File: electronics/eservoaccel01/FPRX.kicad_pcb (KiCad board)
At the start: 2 copper layers, 25 x 37 mm, 83 parts, among them IC1 ST490, IC3 ATMEGA328P-M, K1 CONN_3, K2 CONN_3, K3 CONN_3, K4 CONN_3, P1 CONN_6, P2 CONN_1, X1 RESONATOR_16MHz

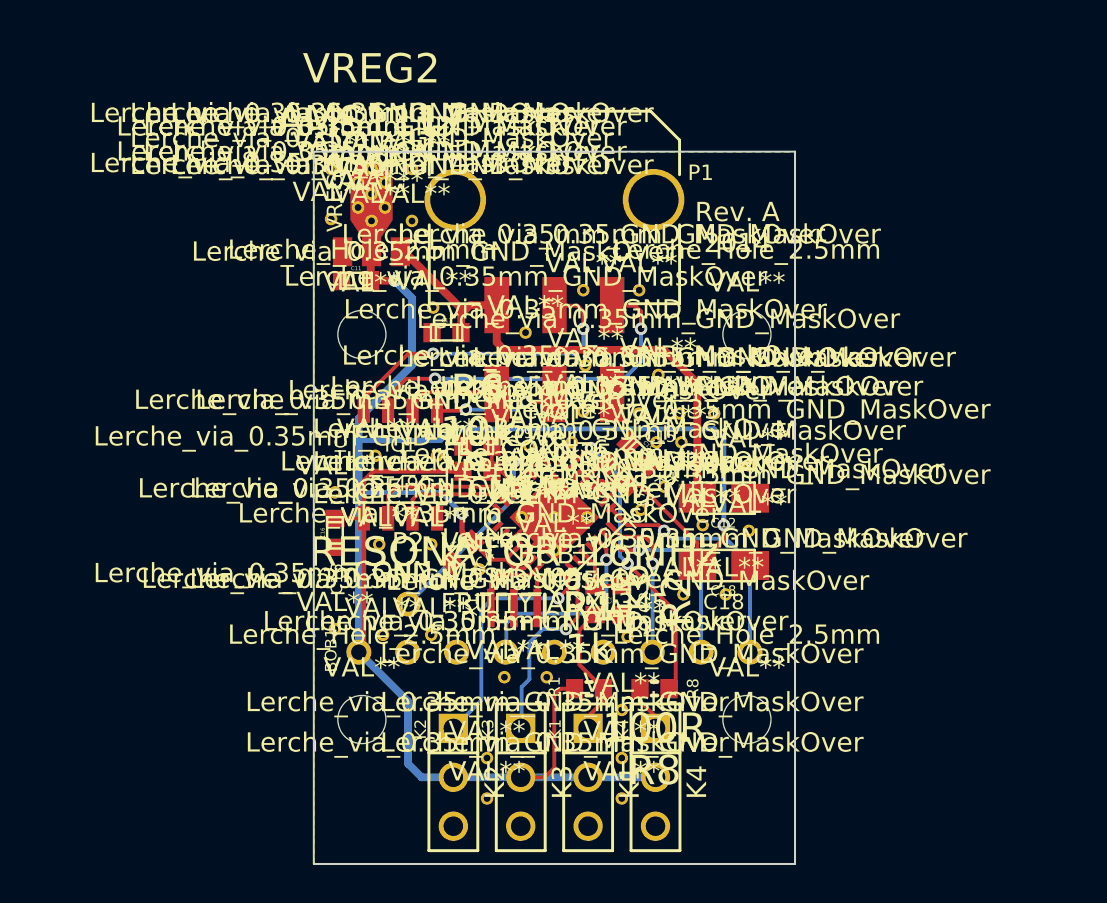
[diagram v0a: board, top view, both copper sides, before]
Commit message: Removed unused components from schematic, added WS2812 LED, changed C18 to C17
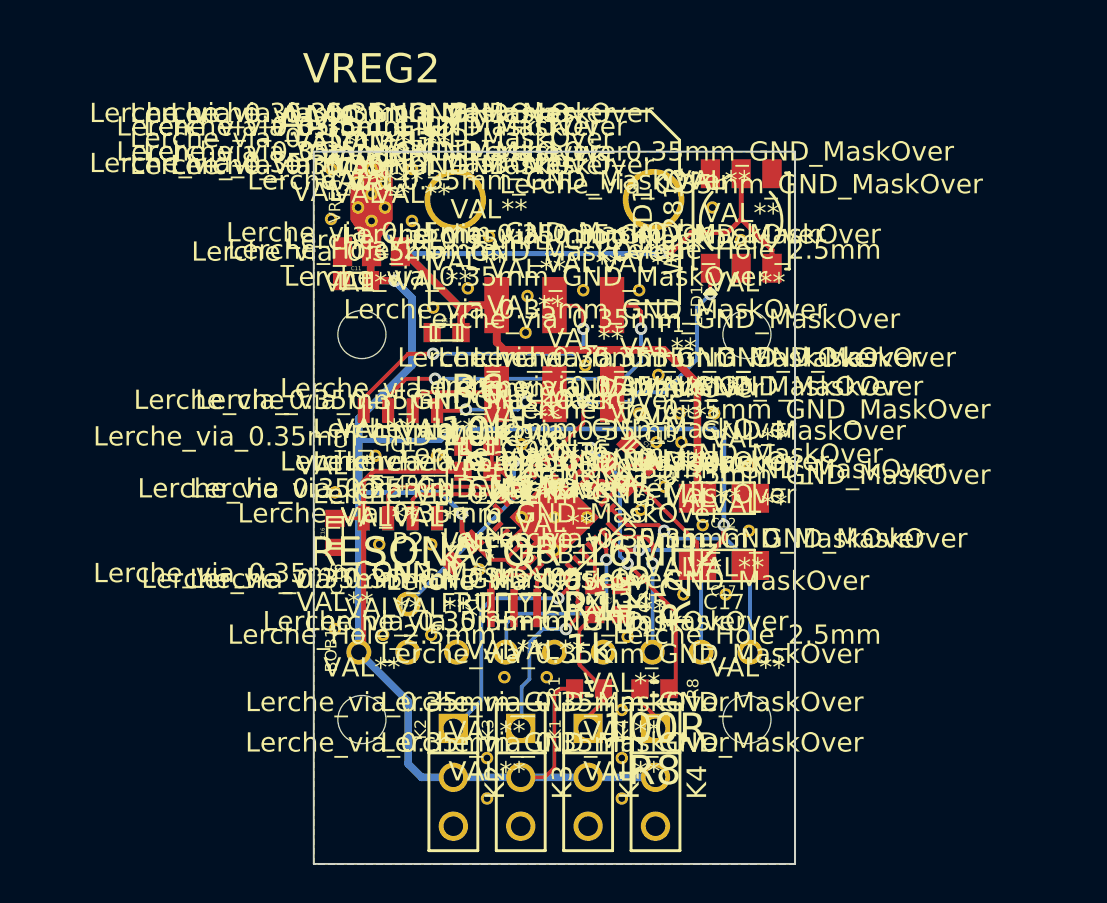
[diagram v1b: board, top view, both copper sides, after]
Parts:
- removed the Lerche_via_0.35mm_GND_MaskOver at (245.0, 138.5)
- removed the Lerche_via_0.35mm_GND_MaskOver at (242.2, 140.3)
- removed the Lerche_via_0.35mm_GND_MaskOver at (244.4, 140.1)
- added LED1: WS2812, Lerche_WS2812, F.Cu at (253.2, 128.6)
- added Lerche_via_0.35mm_GND_MaskOver: VAL**, Lerche_via_0.35mm_GND_MaskOver, F.Cu at (251.7, 127.9)
- added Lerche_via_0.35mm_GND_MaskOver: VAL**, Lerche_via_0.35mm_GND_MaskOver, F.Cu at (253.2, 129.6)
- added Lerche_via_0.35mm_GND_MaskOver: VAL**, Lerche_via_0.35mm_GND_MaskOver, F.Cu at (240.1, 129.4)
- added Lerche_via_0.35mm_GND_MaskOver: VAL**, Lerche_via_0.35mm_GND_MaskOver, F.Cu at (242.1, 132.5)
- added Lerche_via_0.35mm_GND_MaskOver: VAL**, Lerche_via_0.35mm_GND_MaskOver, F.Cu at (239.0, 132.1)
- added Lerche_via_0.35mm_GND_MaskOver: VAL**, Lerche_via_0.35mm_GND_MaskOver, F.Cu at (241.8, 140.2)
- renumbered C18 to C17
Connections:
- IC3 pad 1: N-0000016 (its old number) -> (no net)
- IC3 pad 25: (no net) -> DOUT_STATUS
- IC3 pad 32: N-0000011 -> (no net)
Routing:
- net +5V: track 117.4 -> 143.6 mm, vias 3 -> 4
- net DOUT_STATUS: track 0.00 -> 15.7 mm, vias 0 -> 2
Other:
- board text added: "C17"
- board text added: "LED1"
- board text removed: "C18"
- board text removed: "Rev. A 2014"

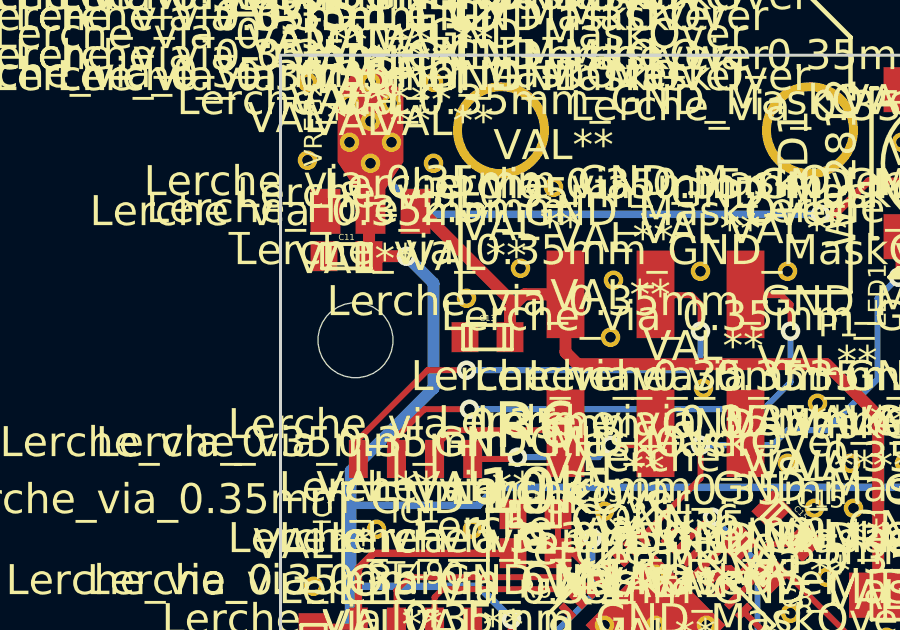
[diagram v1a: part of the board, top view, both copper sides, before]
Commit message: Added reference for C11 & C12
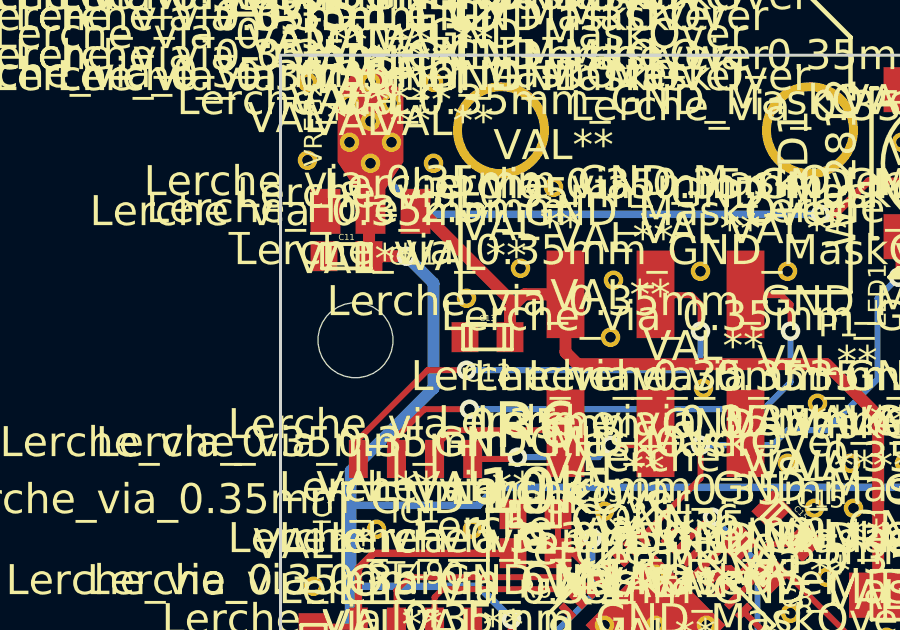
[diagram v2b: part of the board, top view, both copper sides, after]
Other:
- board text added: "C11"
- board text added: "C13"
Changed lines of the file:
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@@
     (links 129)
     (no_connects 0)
-    (area 230.949999 124.949999 256.050001 162.050001)
+    (area 214.998334 119.6256 270.501666 203.1025)
     (thickness 1.6)
-    (drawings 34)
+    (drawings 36)
     (tracks 247)
     (zones 0)
@@
   )
   (setup
-    (last_trace_width 0.254)
+    (last_trace_width 0.16)
     (user_trace_width 0.16)
     (user_trace_width 0.2)
@@
     )
   )
+  (gr_text C13 (at 237.9 135.6) (layer F.SilkS)
+    (effects (font (size 0.6 0.6) (thickness 0.12)))
+  )
+  (gr_text C11 (at 235.4 131.7) (layer F.SilkS)
+    (effects (font (size 0.6 0.6) (thickness 0.12)))
+  )
   (gr_text LED1 (at 250.9 133 90) (layer F.SilkS)

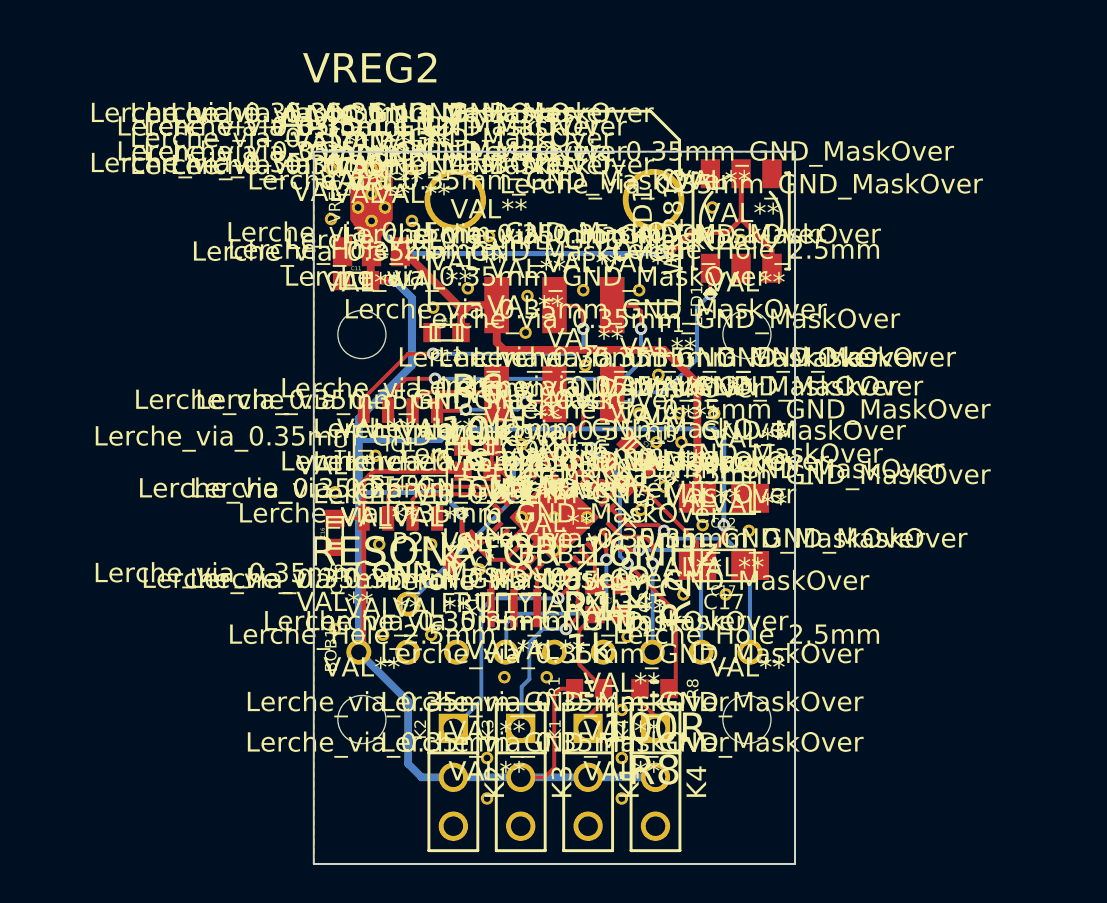
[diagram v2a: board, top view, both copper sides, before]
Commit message: Added resistor for WS2812 onboard LED, connected to the right input
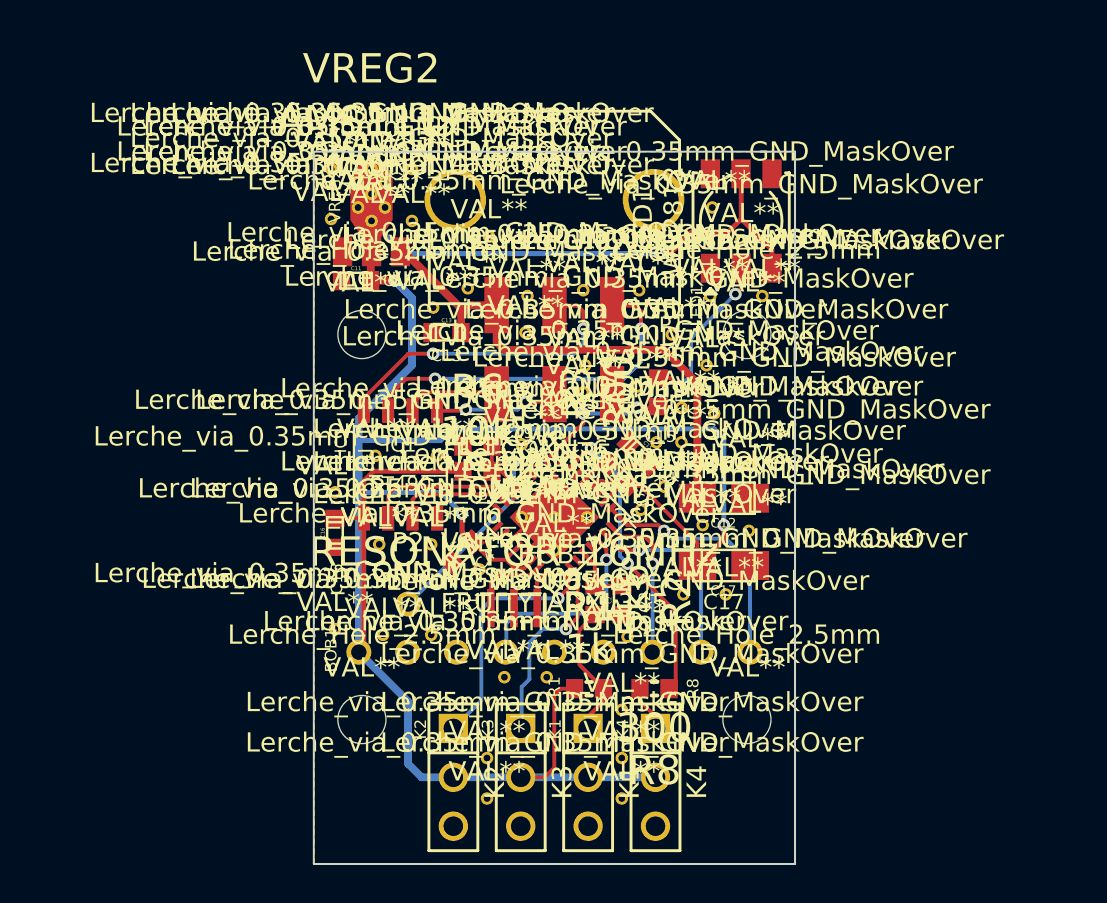
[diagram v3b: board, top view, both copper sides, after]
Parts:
- removed the Lerche_via_0.35mm_GND_MaskOver at (248.9, 136.6)
- removed the Lerche_via_0.35mm_GND_MaskOver at (250.0, 138.6)
- removed the Lerche_via_0.35mm_GND_MaskOver at (247.9, 138.6)
- added Lerche_via_0.35mm_GND_MaskOver: VAL**, Lerche_via_0.35mm_GND_MaskOver, F.Cu at (250.1, 138.3)
- added Lerche_via_0.35mm_GND_MaskOver: VAL**, Lerche_via_0.35mm_GND_MaskOver, F.Cu at (247.8, 137.2)
- added Lerche_via_0.35mm_GND_MaskOver: VAL**, Lerche_via_0.35mm_GND_MaskOver, F.Cu at (245.0, 137.5)
- added Lerche_via_0.35mm_GND_MaskOver: VAL**, Lerche_via_0.35mm_GND_MaskOver, F.Cu at (249.6, 134.5)
- added Lerche_via_0.35mm_GND_MaskOver: VAL**, Lerche_via_0.35mm_GND_MaskOver, F.Cu at (251.4, 136.1)
- added Lerche_via_0.35mm_GND_MaskOver: VAL**, Lerche_via_0.35mm_GND_MaskOver, F.Cu at (251.6, 132.5)
- added Lerche_via_0.35mm_GND_MaskOver: VAL**, Lerche_via_0.35mm_GND_MaskOver, F.Cu at (254.3, 132.5)
- added R3: 300, Lerche_R0603, F.Cu at (248.9, 137.5)
- C17: value 100uF_tantalum -> 22uF_tantalum
- R8: value 100R -> 300
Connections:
- LED1 pad 1: DOUT_STATUS -> (no net)
- LED1 pad 2: (no net) -> N-0000010
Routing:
- net N-0000010: track 0.00 -> 8.76 mm, vias 0 -> 2
- net DOUT_STATUS: track 15.7 -> 7.32 mm
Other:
- board text added: "R3"

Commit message: Redesigned with Micro USB instead of Microfit. PCB is now smaller. Using I2C to communicate with motion controller
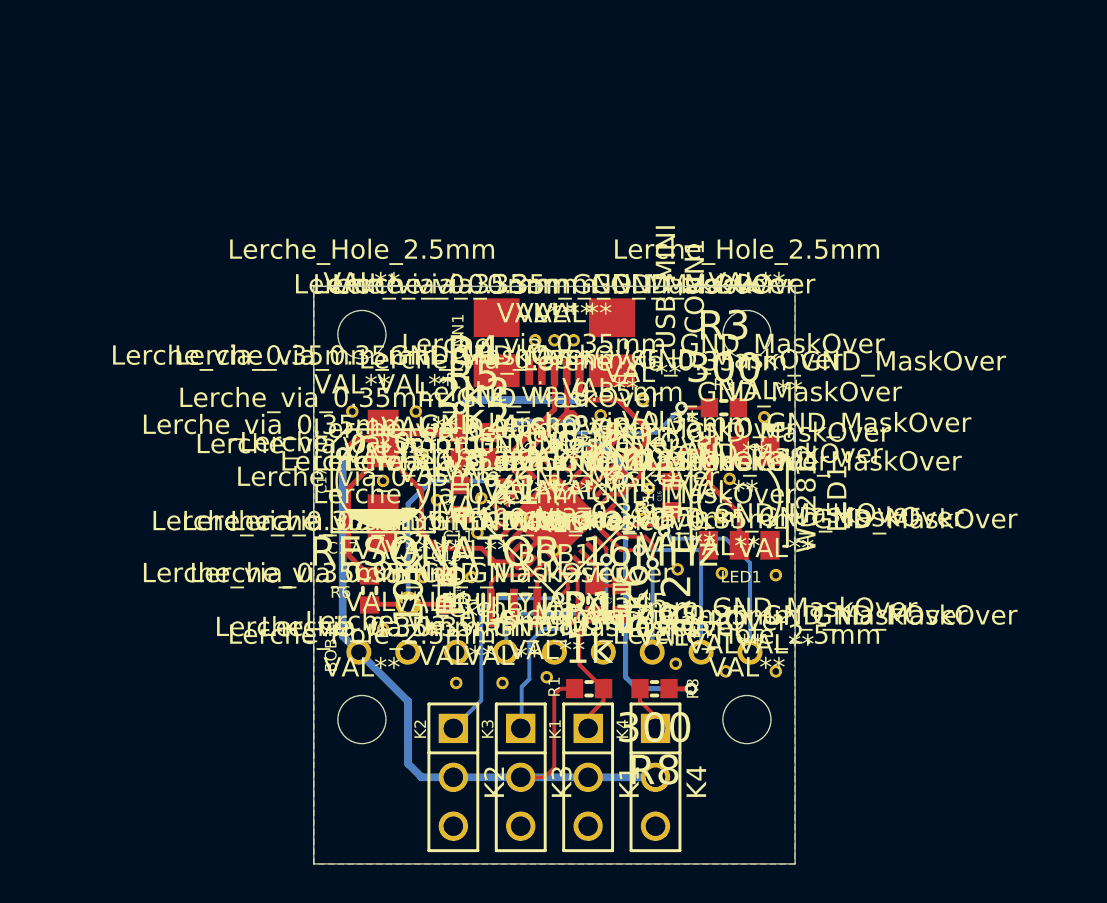
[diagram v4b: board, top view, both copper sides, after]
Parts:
- removed C12: 10uF, c_tant_A
- removed C13, C4: 0.1uF, c_0603
- removed IC1: ST490, so-8
- removed the Lerche_via_0.35mm_GND_MaskOver at (233.3, 127.9)
- removed the Lerche_via_0.35mm_GND_MaskOver at (231.9, 125.9)
- removed the Lerche_via_0.35mm_GND_MaskOver at (231.9, 128.5)
- removed the Lerche_via_0.35mm_GND_MaskOver at (236.1, 125.9)
- removed the Lerche_via_0.35mm_GND_MaskOver at (236.1, 128.6)
- removed the Lerche_via_0.35mm_GND_MaskOver at (237.2, 133.1)
- removed the Lerche_via_0.35mm_GND_MaskOver at (242.0, 134.4)
- removed the Lerche_via_0.35mm_GND_MaskOver at (233.3, 126.6)
- removed the Lerche_via_0.35mm_GND_MaskOver at (245.1, 136.1)
- removed the Lerche_via_0.35mm_GND_MaskOver at (247.3, 150.2)
- removed the Lerche_via_0.35mm_GND_MaskOver at (240.9, 152.3)
- removed the Lerche_via_0.35mm_GND_MaskOver at (250.2, 148.0)
- removed the Lerche_via_0.35mm_GND_MaskOver at (252.4, 148.0)
- removed the Lerche_via_0.35mm_GND_MaskOver at (253.6, 144.7)
- removed the Lerche_via_0.35mm_GND_MaskOver at (251.8, 138.6)
- removed the Lerche_via_0.35mm_GND_MaskOver at (245.0, 132.2)
- removed the Lerche_via_0.35mm_GND_MaskOver at (247.9, 132.2)
- removed the Lerche_via_0.35mm_GND_MaskOver at (234.7, 126.6)
- removed the Lerche_via_0.35mm_GND_MaskOver at (234.6, 150.1)
- removed the Lerche_via_0.35mm_GND_MaskOver at (237.1, 150.1)
- removed the Lerche_via_0.35mm_GND_MaskOver at (232.1, 149.8)
- removed the Lerche_via_0.35mm_GND_MaskOver at (232.1, 142.7)
- removed the Lerche_via_0.35mm_GND_MaskOver at (234.2, 140.8)
- removed the Lerche_via_0.35mm_GND_MaskOver at (237.4, 140.8)
- removed the Lerche_via_0.35mm_GND_MaskOver at (240.0, 156.5)
- removed the Lerche_via_0.35mm_GND_MaskOver at (247.0, 156.5)
- removed the Lerche_via_0.35mm_GND_MaskOver at (240.0, 158.6)
- removed the Lerche_via_0.35mm_GND_MaskOver at (247.0, 158.6)
- removed the Lerche_via_0.35mm_GND_MaskOver at (234.0, 128.6)
- removed the Lerche_via_0.35mm_GND_MaskOver at (247.0, 154.0)
- removed the Lerche_via_0.35mm_GND_MaskOver at (253.6, 141.3)
- removed the Lerche_via_0.35mm_GND_MaskOver at (248.8, 140.1)
- removed the Lerche_via_0.35mm_GND_MaskOver at (249.2, 142.4)
- removed the Lerche_via_0.35mm_GND_MaskOver at (251.2, 144.4)
- removed the Lerche_via_0.35mm_GND_MaskOver at (234.4, 145.4)
- removed the Lerche_via_0.35mm_GND_MaskOver at (250.1, 140.1)
- removed the Lerche_via_0.35mm_GND_MaskOver at (234.0, 125.9)
- removed the Lerche_via_0.35mm_GND_MaskOver at (251.7, 127.9)
- removed the Lerche_via_0.35mm_GND_MaskOver at (234.0, 127.2)
- removed the Lerche_via_0.35mm_GND_MaskOver at (253.2, 129.6)
- removed the Lerche_via_0.35mm_GND_MaskOver at (240.1, 129.4)
- removed the Lerche_via_0.35mm_GND_MaskOver at (242.1, 132.5)
- removed the Lerche_via_0.35mm_GND_MaskOver at (239.0, 132.1)
- removed the Lerche_via_0.35mm_GND_MaskOver at (241.8, 140.2)
- removed the Lerche_via_0.35mm_GND_MaskOver at (250.1, 138.3)
- removed the Lerche_via_0.35mm_GND_MaskOver at (247.8, 137.2)
- removed the Lerche_via_0.35mm_GND_MaskOver at (245.0, 137.5)
- removed the Lerche_via_0.35mm_GND_MaskOver at (249.6, 134.5)
- removed the Lerche_via_0.35mm_GND_MaskOver at (251.4, 136.1)
- removed the Lerche_via_0.35mm_GND_MaskOver at (234.7, 127.9)
- removed the Lerche_via_0.35mm_GND_MaskOver at (251.6, 132.5)
- removed the Lerche_via_0.35mm_GND_MaskOver at (254.3, 132.5)
- removed the Lerche_via_0.35mm_GND_MaskOver at (237.1, 145.4)
- removed the Lerche_via_0.35mm_GND_MaskOver at (239.6, 146.7)
- removed P1: CONN_6, Lerche_Molex_Microfit_0430450607
- removed VREG2: AMS1117, Lerche_SOT89
- added CONN1: USB_MINI, Lerche_Molex_47610-0001_Micro-USB, F.Cu at (243.5, 132.0)
- added Lerche_via_0.35mm_GND_MaskOver: VAL**, Lerche_via_0.35mm_GND_MaskOver, F.Cu at (235.1, 147.1)
- added Lerche_via_0.35mm_GND_MaskOver: VAL**, Lerche_via_0.35mm_GND_MaskOver, F.Cu at (240.8, 152.6)
- added Lerche_via_0.35mm_GND_MaskOver: VAL**, Lerche_via_0.35mm_GND_MaskOver, F.Cu at (245.9, 138.7)
- added Lerche_via_0.35mm_GND_MaskOver: VAL**, Lerche_via_0.35mm_GND_MaskOver, F.Cu at (248.1, 137.9)
- added Lerche_via_0.35mm_GND_MaskOver: VAL**, Lerche_via_0.35mm_GND_MaskOver, F.Cu at (249.0, 140.4)
- added Lerche_via_0.35mm_GND_MaskOver: VAL**, Lerche_via_0.35mm_GND_MaskOver, F.Cu at (254.4, 138.8)
- added Lerche_via_0.35mm_GND_MaskOver: VAL**, Lerche_via_0.35mm_GND_MaskOver, F.Cu at (252.6, 142.0)
- added Lerche_via_0.35mm_GND_MaskOver: VAL**, Lerche_via_0.35mm_GND_MaskOver, F.Cu at (252.1, 144.0)
- added Lerche_via_0.35mm_GND_MaskOver: VAL**, Lerche_via_0.35mm_GND_MaskOver, F.Cu at (236.5, 140.7)
- added Lerche_via_0.35mm_GND_MaskOver: VAL**, Lerche_via_0.35mm_GND_MaskOver, F.Cu at (234.6, 142.1)
- added Lerche_via_0.35mm_GND_MaskOver: VAL**, Lerche_via_0.35mm_GND_MaskOver, F.Cu at (234.6, 149.8)
- added Lerche_via_0.35mm_GND_MaskOver: VAL**, Lerche_via_0.35mm_GND_MaskOver, F.Cu at (237.1, 149.8)
- added Lerche_via_0.35mm_GND_MaskOver: VAL**, Lerche_via_0.35mm_GND_MaskOver, F.Cu at (238.4, 152.6)
- added Lerche_via_0.35mm_GND_MaskOver: VAL**, Lerche_via_0.35mm_GND_MaskOver, F.Cu at (249.9, 146.7)
- added Lerche_via_0.35mm_GND_MaskOver: VAL**, Lerche_via_0.35mm_GND_MaskOver, F.Cu at (252.2, 146.9)
- added Lerche_via_0.35mm_GND_MaskOver: VAL**, Lerche_via_0.35mm_GND_MaskOver, F.Cu at (255.0, 147.0)
- added Lerche_via_0.35mm_GND_MaskOver: VAL**, Lerche_via_0.35mm_GND_MaskOver, F.Cu at (248.4, 142.5)
- added Lerche_via_0.35mm_GND_MaskOver: VAL**, Lerche_via_0.35mm_GND_MaskOver, F.Cu at (236.3, 138.5)
- added Lerche_via_0.35mm_GND_MaskOver: VAL**, Lerche_via_0.35mm_GND_MaskOver, F.Cu at (233.0, 138.5)
- added Lerche_via_0.35mm_GND_MaskOver: VAL**, Lerche_via_0.35mm_GND_MaskOver, F.Cu at (252.4, 152.0)
- added Lerche_via_0.35mm_GND_MaskOver: VAL**, Lerche_via_0.35mm_GND_MaskOver, F.Cu at (249.8, 151.6)
- added Lerche_via_0.35mm_GND_MaskOver: VAL**, Lerche_via_0.35mm_GND_MaskOver, F.Cu at (255.0, 152.0)
- added Lerche_via_0.35mm_GND_MaskOver: VAL**, Lerche_via_0.35mm_GND_MaskOver, F.Cu at (243.5, 134.8)
- added Lerche_via_0.35mm_GND_MaskOver: VAL**, Lerche_via_0.35mm_GND_MaskOver, F.Cu at (244.5, 134.8)
- added Lerche_via_0.35mm_GND_MaskOver: VAL**, Lerche_via_0.35mm_GND_MaskOver, F.Cu at (242.5, 134.8)
- added Lerche_via_0.35mm_GND_MaskOver: VAL**, Lerche_via_0.35mm_GND_MaskOver, F.Cu at (239.7, 143.0)
- added Lerche_via_0.35mm_GND_MaskOver: VAL**, Lerche_via_0.35mm_GND_MaskOver, F.Cu at (237.4, 143.1)
- added Lerche_via_0.35mm_GND_MaskOver: VAL**, Lerche_via_0.35mm_GND_MaskOver, F.Cu at (239.5, 144.8)
- added Lerche_via_0.35mm_GND_MaskOver: VAL**, Lerche_via_0.35mm_GND_MaskOver, F.Cu at (239.2, 147.1)
- added Lerche_via_0.35mm_GND_MaskOver: VAL**, Lerche_via_0.35mm_GND_MaskOver, F.Cu at (236.7, 147.1)
- added R4: 2k2, Lerche_R0603, F.Cu at (239.3, 139.6)
- added R5: 2k2, Lerche_R0603, F.Cu at (239.3, 140.9)
- C17: value 22uF_tantalum -> 100uF; footprint c_tant_A -> c_elec_5x5.8
- moved C17 18.2 mm to (234.6, 142.1), turned to 90 degrees
- moved C16 17.6 mm to (249.6, 142.9)
- moved LED1 14.4 mm to (253.1, 143.0), turned to 270 degrees
- moved C11 12.6 mm to (238.6, 143.1), turned to 90 degrees
- moved R6 8.35 mm to (233.9, 147.8), turned to 270 degrees
- moved C19 7.67 mm to (237.9, 147.8), turned to 270 degrees
- moved R3 3.49 mm to (252.3, 138.3), turned to 0 degrees
- moved C15 1.87 mm to (246.1, 141.2)
- moved C8 1.51 mm to (247.0, 140.3)
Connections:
- IC3 pad 27: (no net) -> SDA
- IC3 pad 28: (no net) -> SCL
- IC3 pad 30: RXD -> (no net)
- IC3 pad 31: TXD -> (no net)
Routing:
- net +5V: track 143.6 -> 97.5 mm, vias 4 -> 3
- net +12V: track 26.8 -> 0.00 mm
- net N-0000023: track 18.9 -> 0.00 mm, vias 2 -> 0
- net N-0000021: track 16.6 -> 0.00 mm, vias 2 -> 0
- net SDA: track 0.00 -> 12.5 mm, vias 0 -> 2
- net SCL: track 0.00 -> 8.14 mm
- net RXD: track 7.98 -> 0.00 mm
- net N-0000014: track 8.76 -> 2.27 mm, vias 2 -> 0
- net N-0000019: track 6.45 -> 0.00 mm, vias 2 -> 0
- net TXD: track 6.03 -> 0.00 mm
- net N-0000020: track 5.03 -> 0.00 mm
- net N-000008: track 16.7 -> 20.1 mm
- net DOUT_STATUS: track 7.32 -> 9.89 mm
- net N-0000018: track 3.74 -> 1.57 mm
- net ~RESET: track 13.6 -> 15.6 mm
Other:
- board size 25 x 37 mm -> 25 x 30 mm
- board text added: "CONN1"
- board text removed: "C12"
- board text removed: "C13"
- board text removed: "C4"
- board text removed: "IC1"
- board text removed: "P1"
- board text removed: "VREG2"
